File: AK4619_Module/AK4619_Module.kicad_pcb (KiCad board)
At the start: 4 copper layers, 58 x 62 mm, 58 parts, among them J1 Conn_01x02, J2 AudioJack2_Ground, J3 AudioJack2_Ground, J4 Conn_01x11, J5 AudioJack2_Ground, J6 AudioJack2_Ground, SW1 SKRPABE010, U1 AP7361EA-33E-13, U2 AK4619VN, U3 ADM811TARTZ

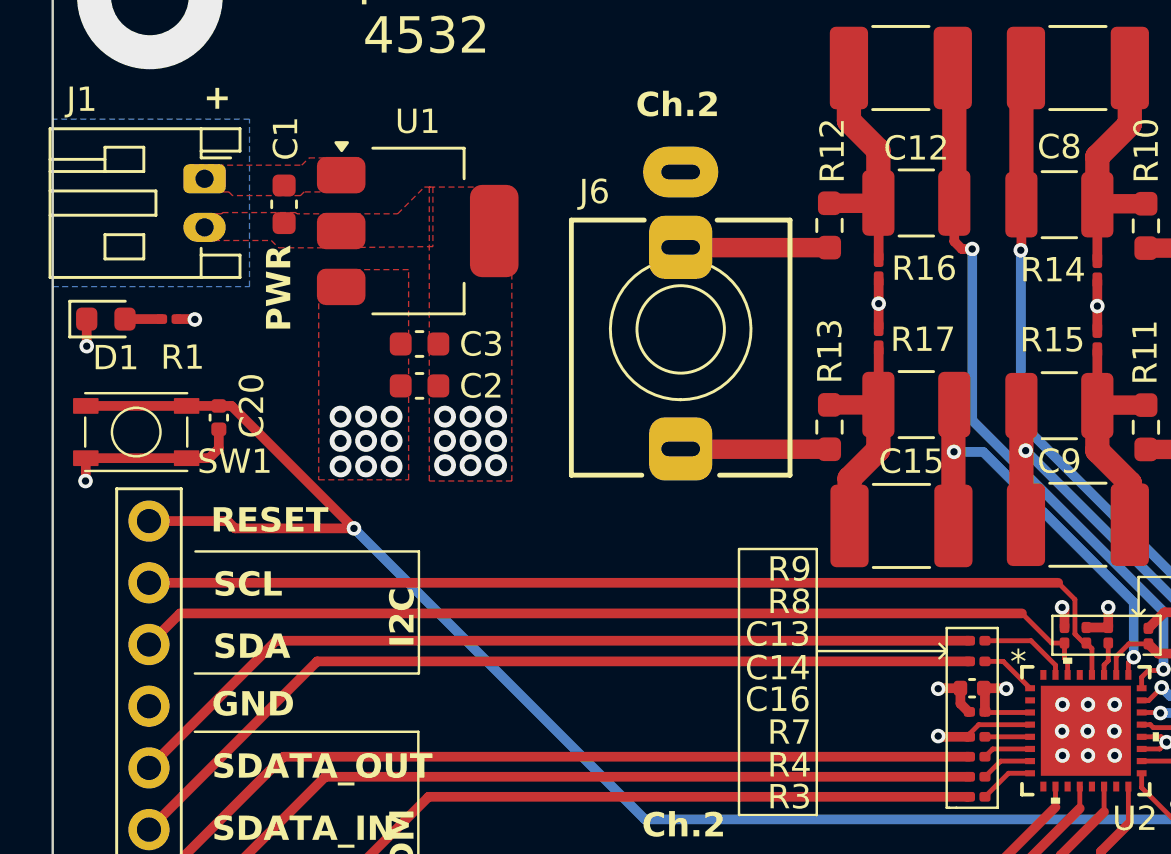
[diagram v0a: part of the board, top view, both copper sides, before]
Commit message: Change the 3D model data path settings.
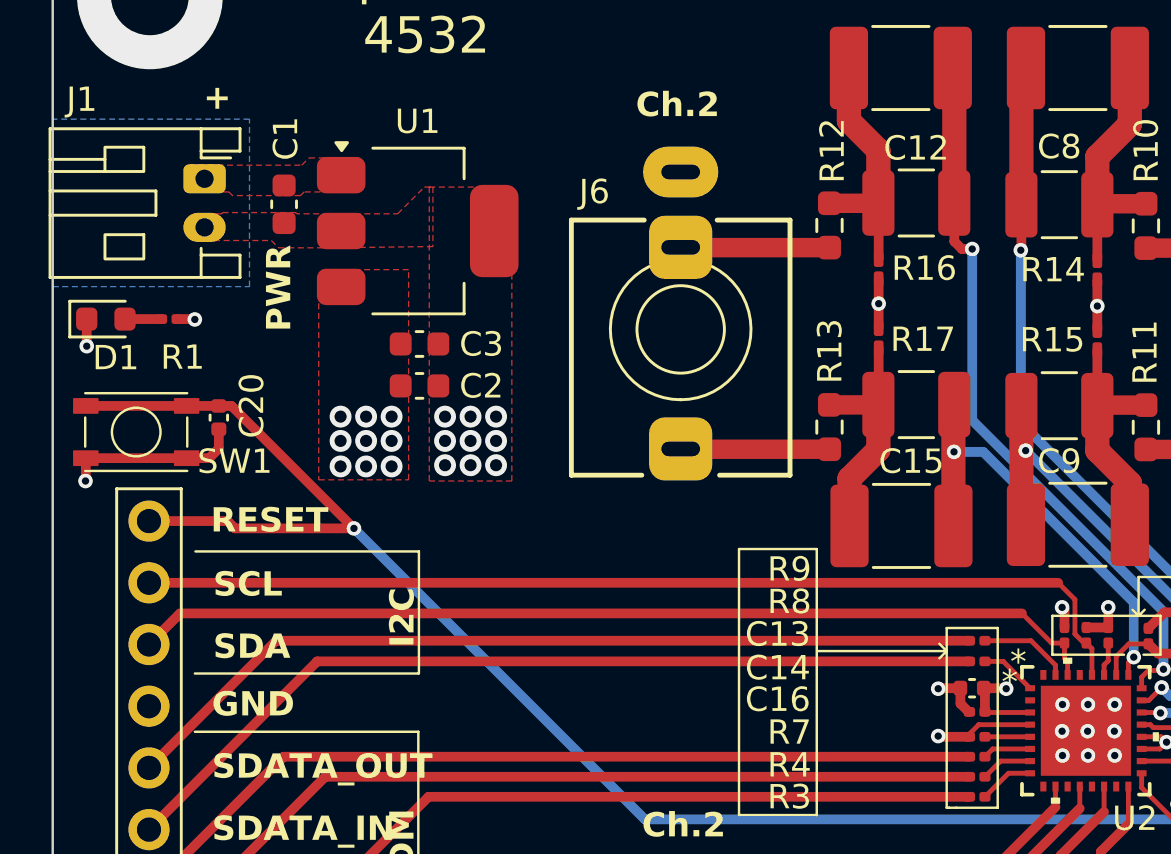
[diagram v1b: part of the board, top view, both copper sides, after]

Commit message: Add dimension annotations
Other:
- board text added: "UNIT: mm t: 1.6"
